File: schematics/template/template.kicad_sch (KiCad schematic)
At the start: 9 parts, among them J1 Bus, J2 Bus, J3 IC-TL, J4 IC-BL, J5 IC-TR, J6 IC-BR

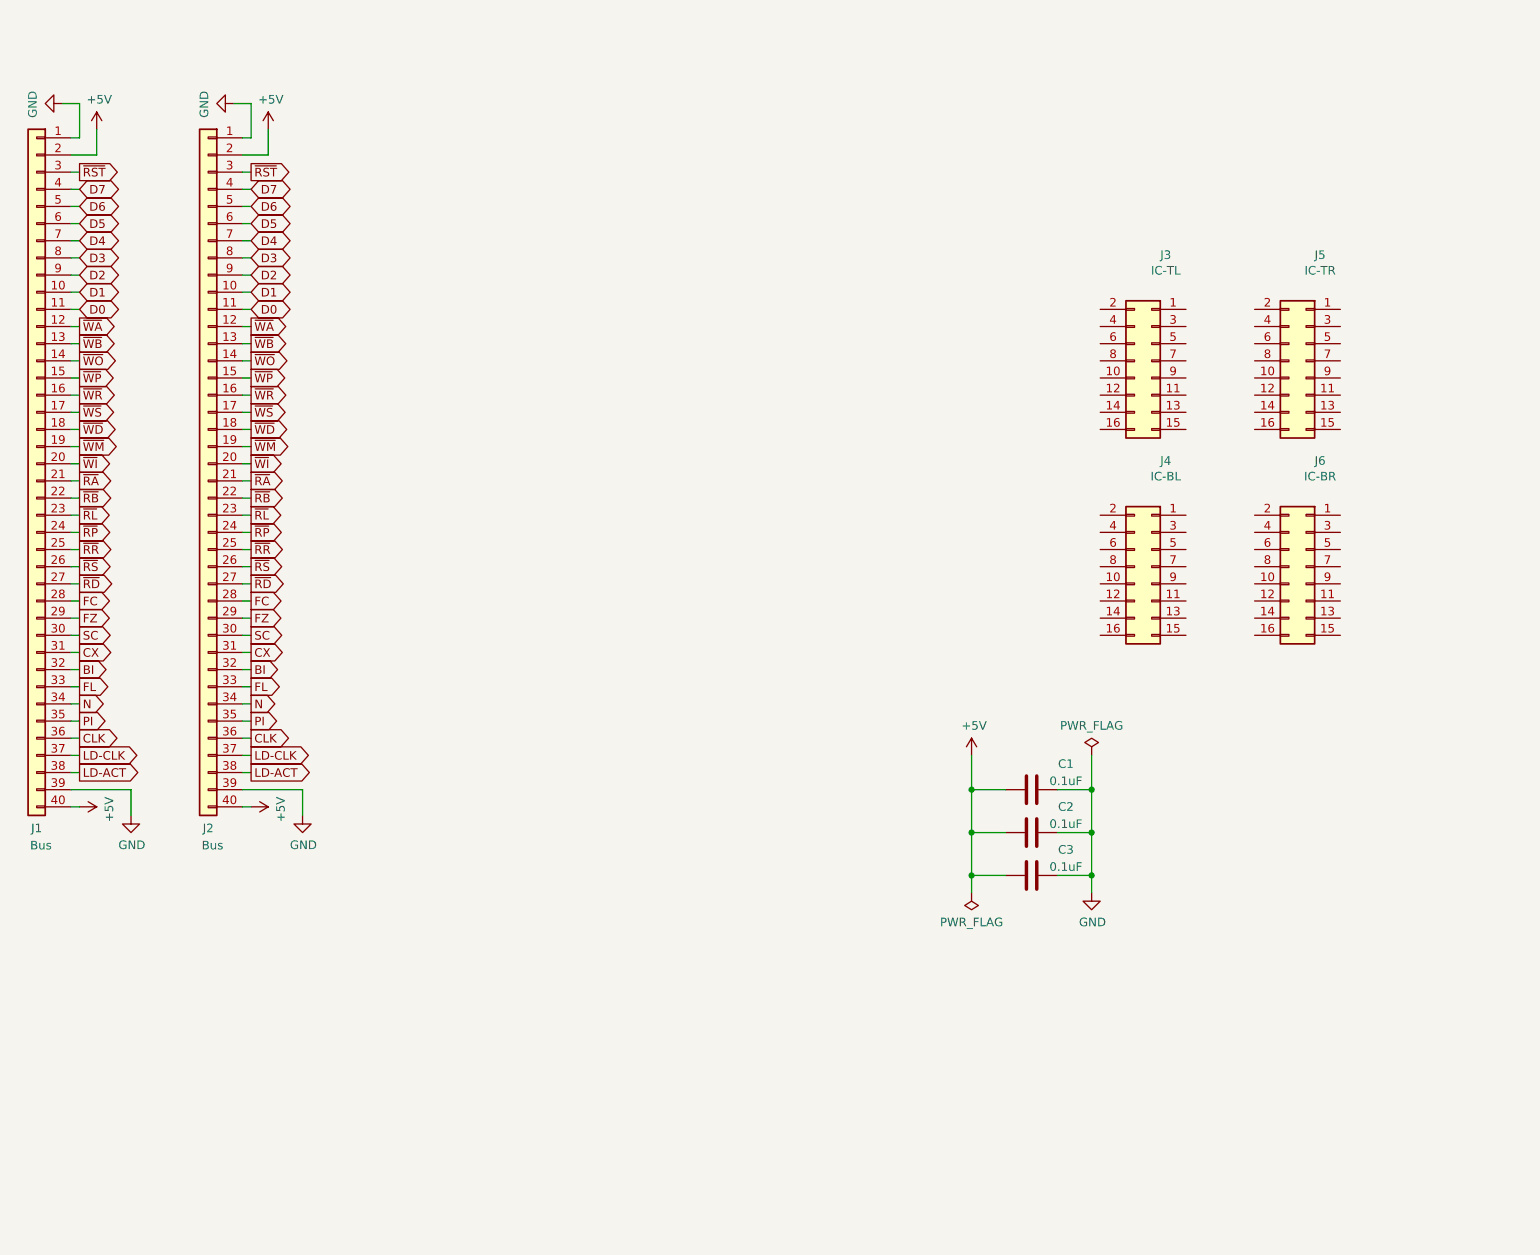
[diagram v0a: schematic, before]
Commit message: update template schematic and docs with interconnect notes
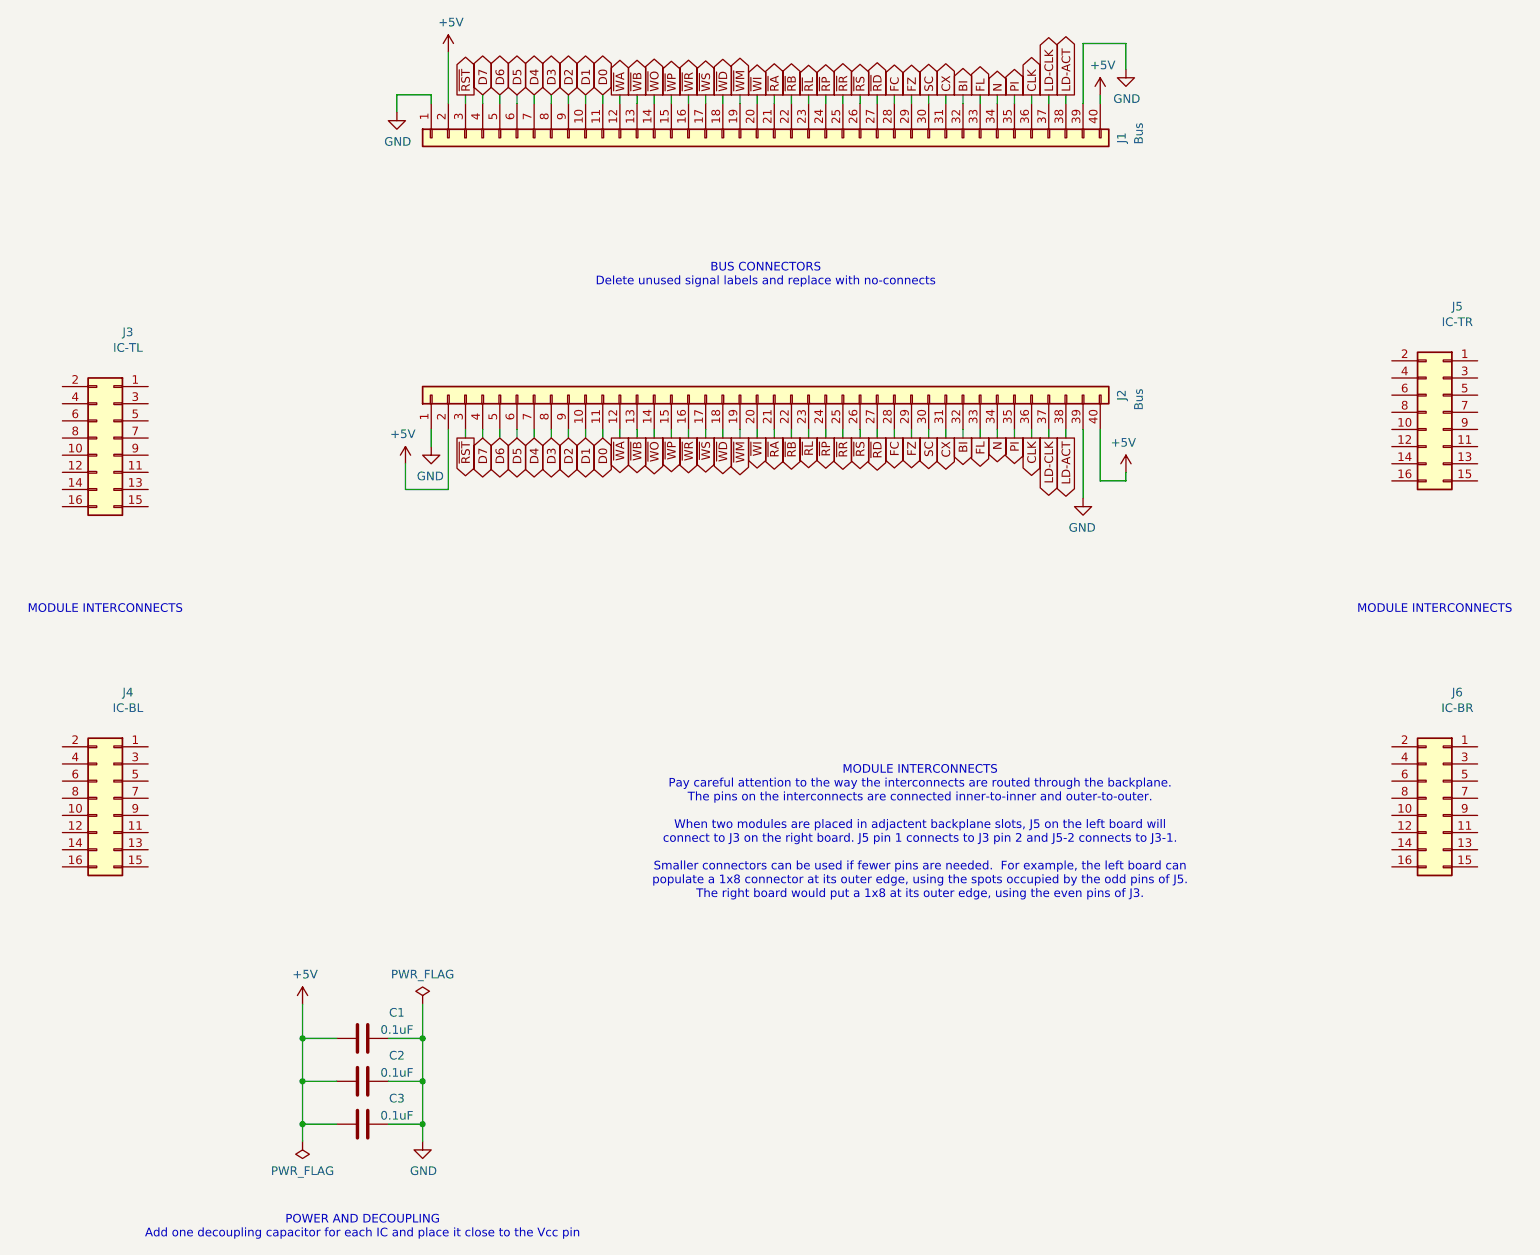
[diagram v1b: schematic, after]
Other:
- note added: "BUS CONNECTORS Delete unused signal labels and replace with no-connects"
- note added: "MODULE INTERCONNECTS"
- note added: "MODULE INTERCONNECTS Pay careful attention to the way the interconnects are routed through the backplane. The pins on the interconnects are connected inner-to-inner and outer-to-outer. When two modules are placed in adjactent backplane slots, J5 on the left board will connect to J3 on the right board. J5 pin 1 connects to J3 pin 2 and J5-2 connects to J3-1. Smaller connectors can be used if fewer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"
- note added: "POWER AND DECOUPLING Add one decoupling capacitor for each IC and place it close to the Vcc pin"
- company: (none) -> github.com/TomNisbet/sap-plus
- title: (none) -> Module Template
- moved on the sheet: C1, C2, C3, J1, J2, J3, J4, J5, J6
